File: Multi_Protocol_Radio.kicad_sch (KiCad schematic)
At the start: 6 parts, among them J2001 TC2050, J2002 Conn_01x06_Pin, J2003 Conn_01x06_Pin, U2001 MGM240PB32VNA3

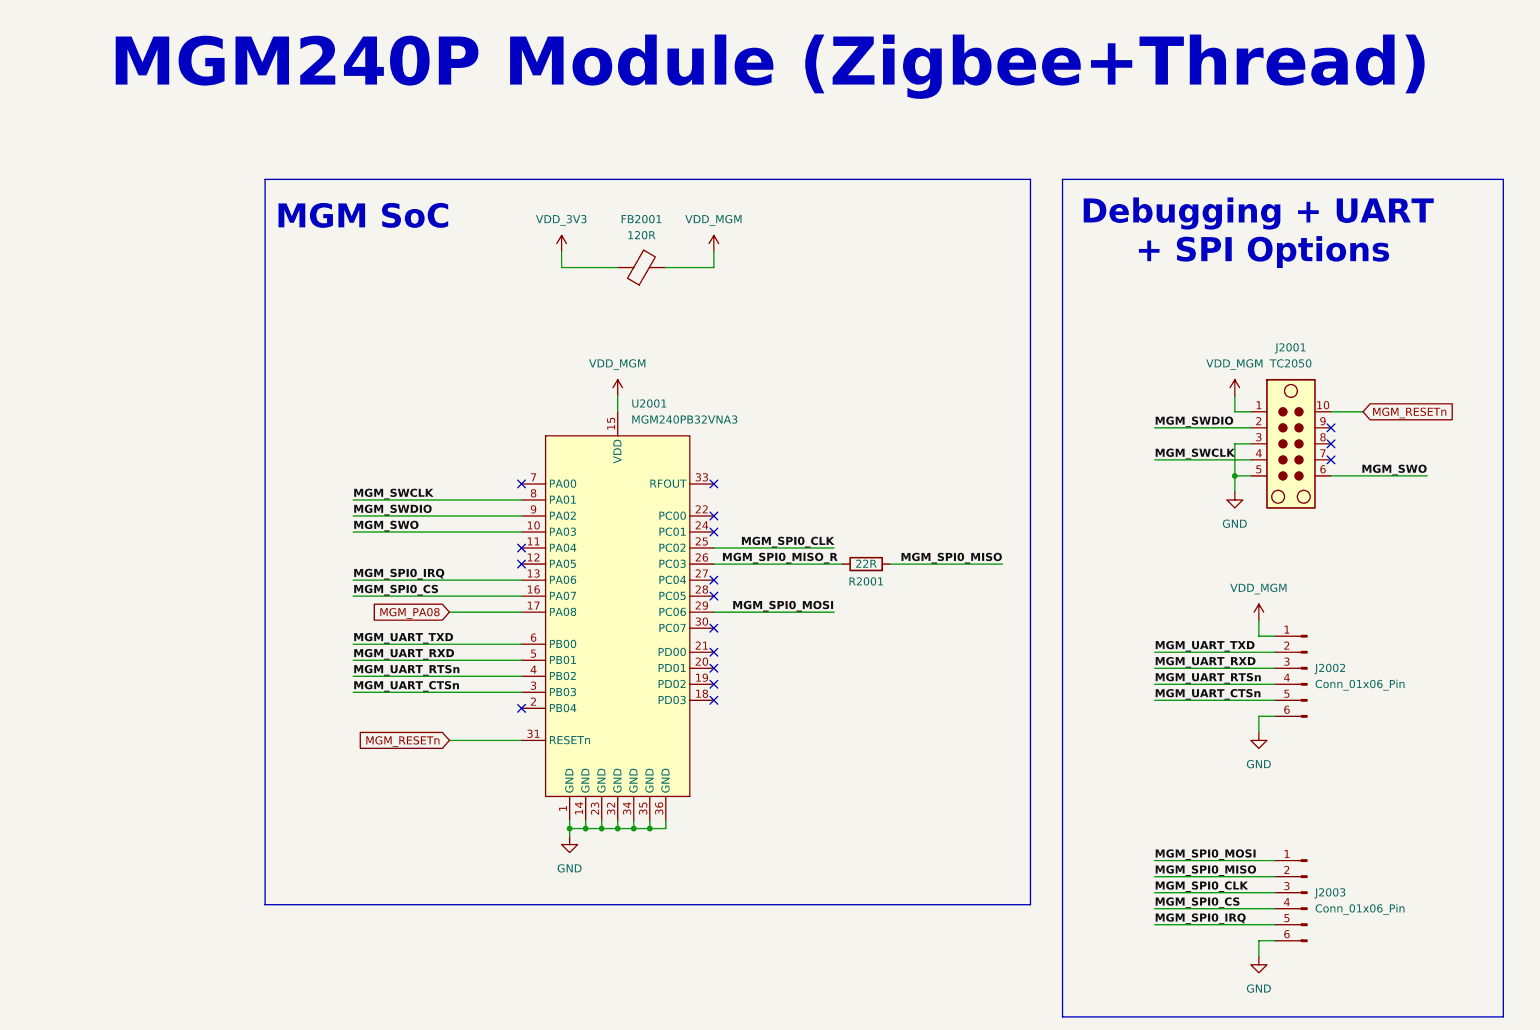
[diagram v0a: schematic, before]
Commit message: All JLC part numbers added to BOM except LEDs
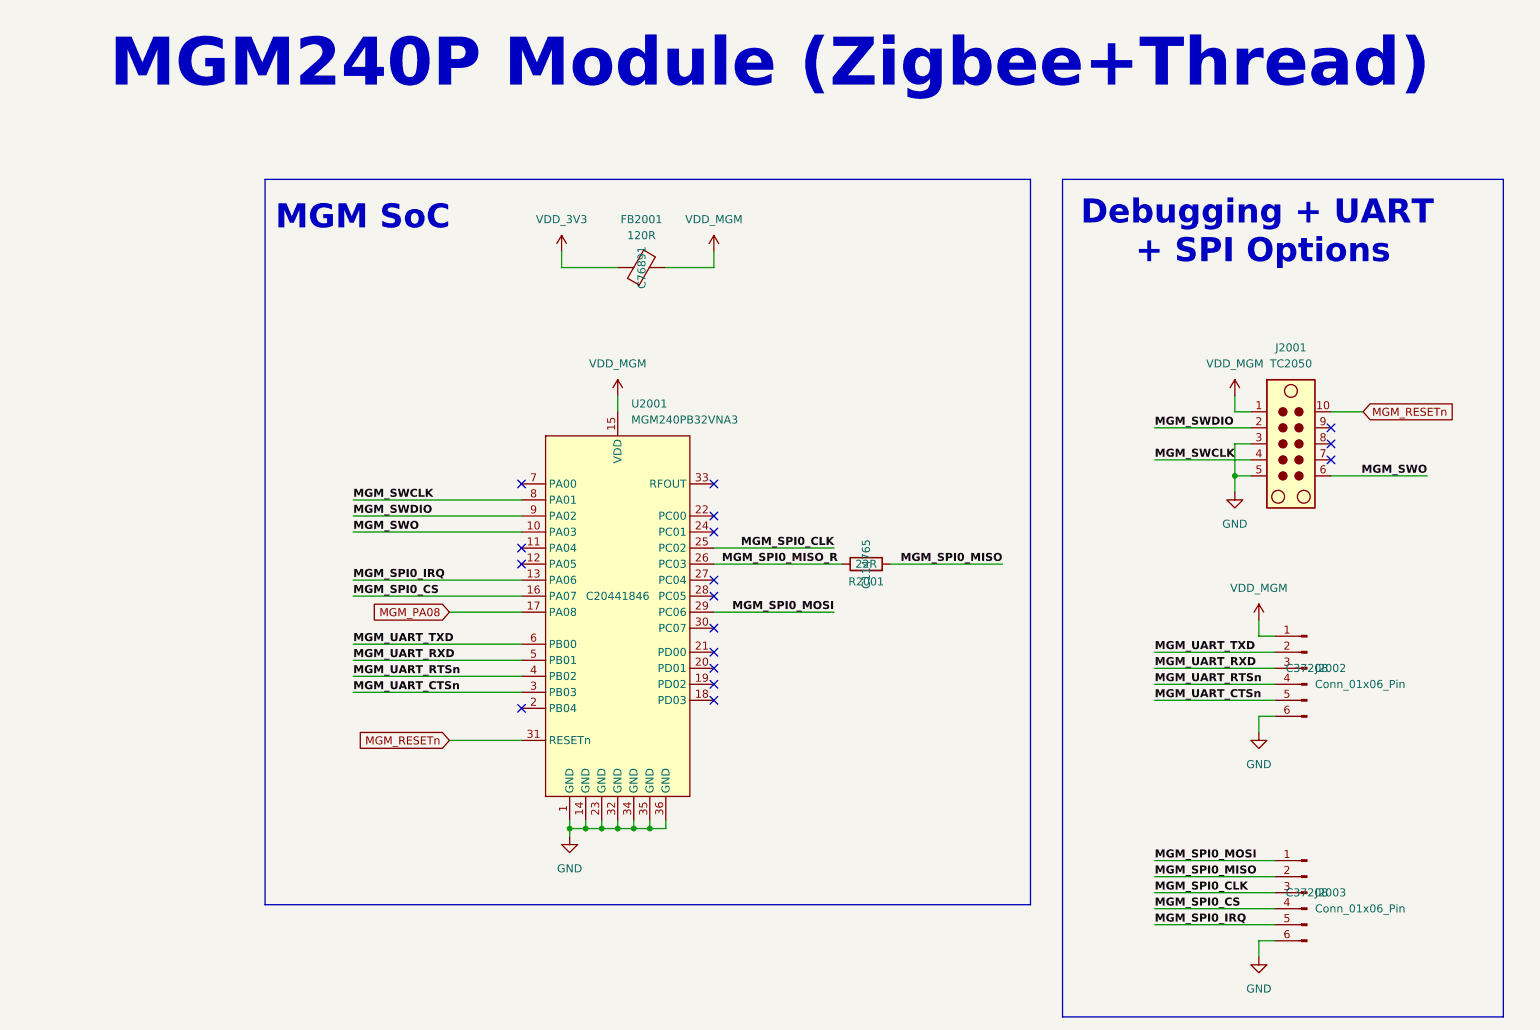
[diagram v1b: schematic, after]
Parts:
- FB2001: JLCPCB Part# (none) -> C76891
- J2002, J2003: JLCPCB Part# (none) -> C37208
- R2001: JLCPCB Part# (none) -> C114765
- U2001: JLCPCB Part# (none) -> C20441846
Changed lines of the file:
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@@
 			)
 		)
-		(property "JLCPCB Part#" ""
+		(property "JLCPCB Part#" "C37208"
 			(at 214.63 158.75 0)
 			(effects
@@
 			)
 		)
-		(property "JLCPCB Part#" ""
+		(property "JLCPCB Part#" "C20441846"
 			(at 105.41 111.76 0)
 			(effects
@@
 			)
 		)
-		(property "JLCPCB Part#" ""
+		(property "JLCPCB Part#" "C76891"
 			(at 109.22 59.69 0)
 			(effects
@@
 			)
 		)
-		(property "JLCPCB Part#" ""
+		(property "JLCPCB Part#" "C37208"
 			(at 214.63 123.19 0)
 			(effects
@@
 			)
 		)
-		(property "JLCPCB Part#" ""
+		(property "JLCPCB Part#" "C114765"
 			(at 144.78 106.68 0)
 			(effects

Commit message: Small DDR4 cleanup
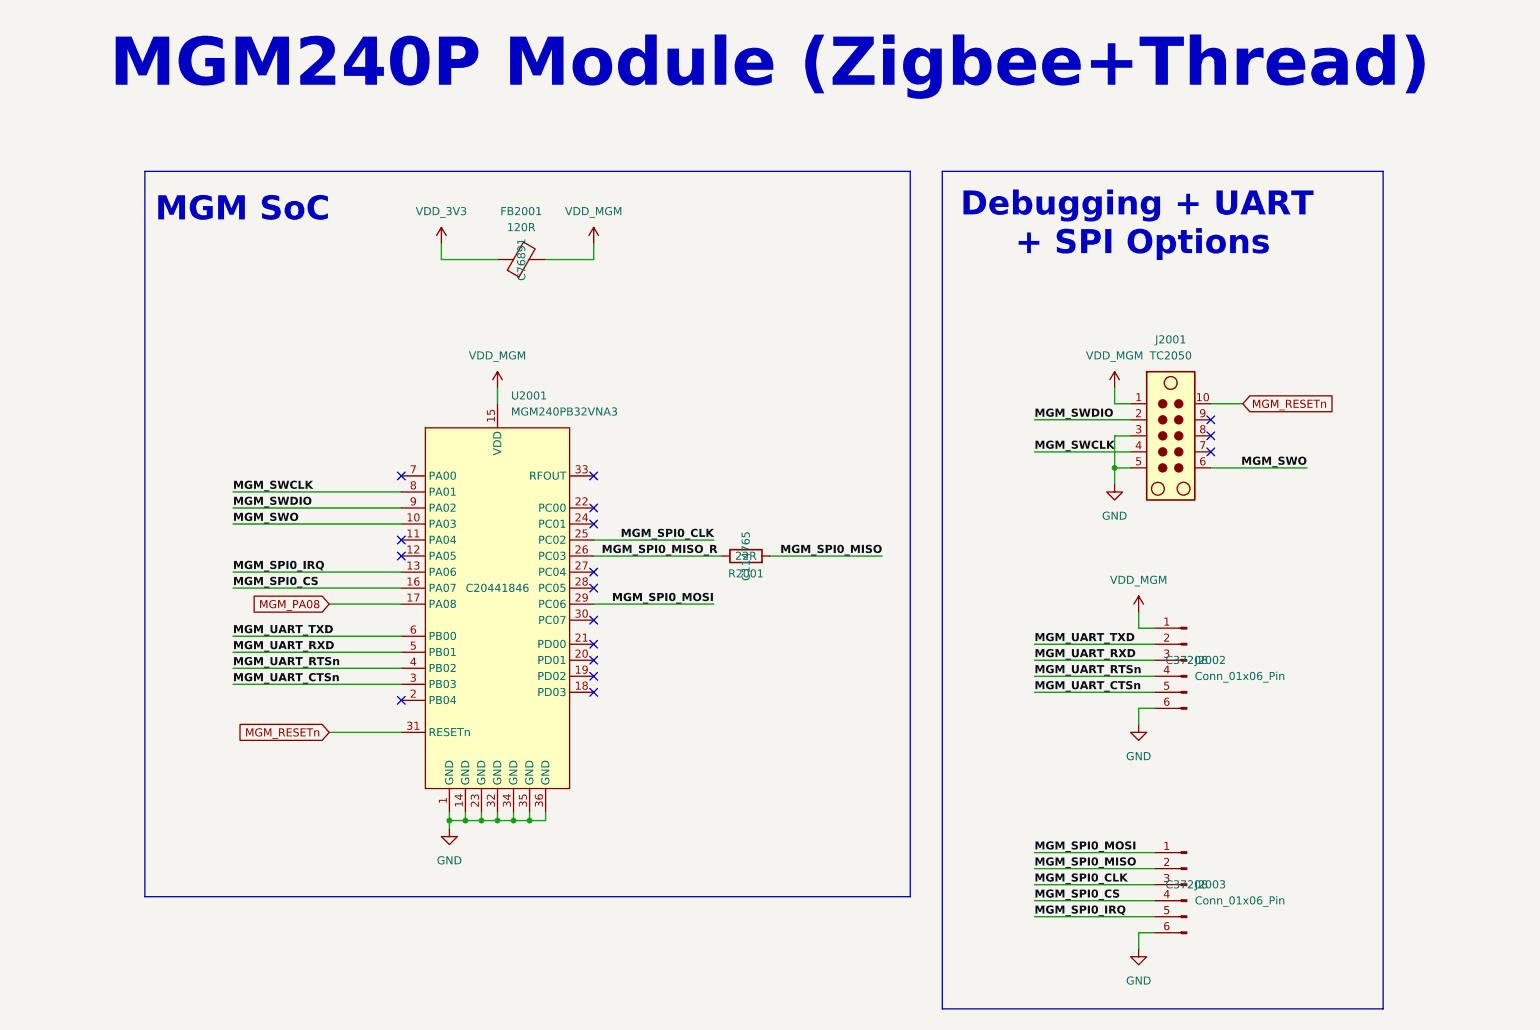
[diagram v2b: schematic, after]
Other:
- moved on the sheet: FB2001, J2001, J2002, J2003, R2001, U2001

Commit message: Added extra decoupling capacitors and pull up resistor to MGM240P module
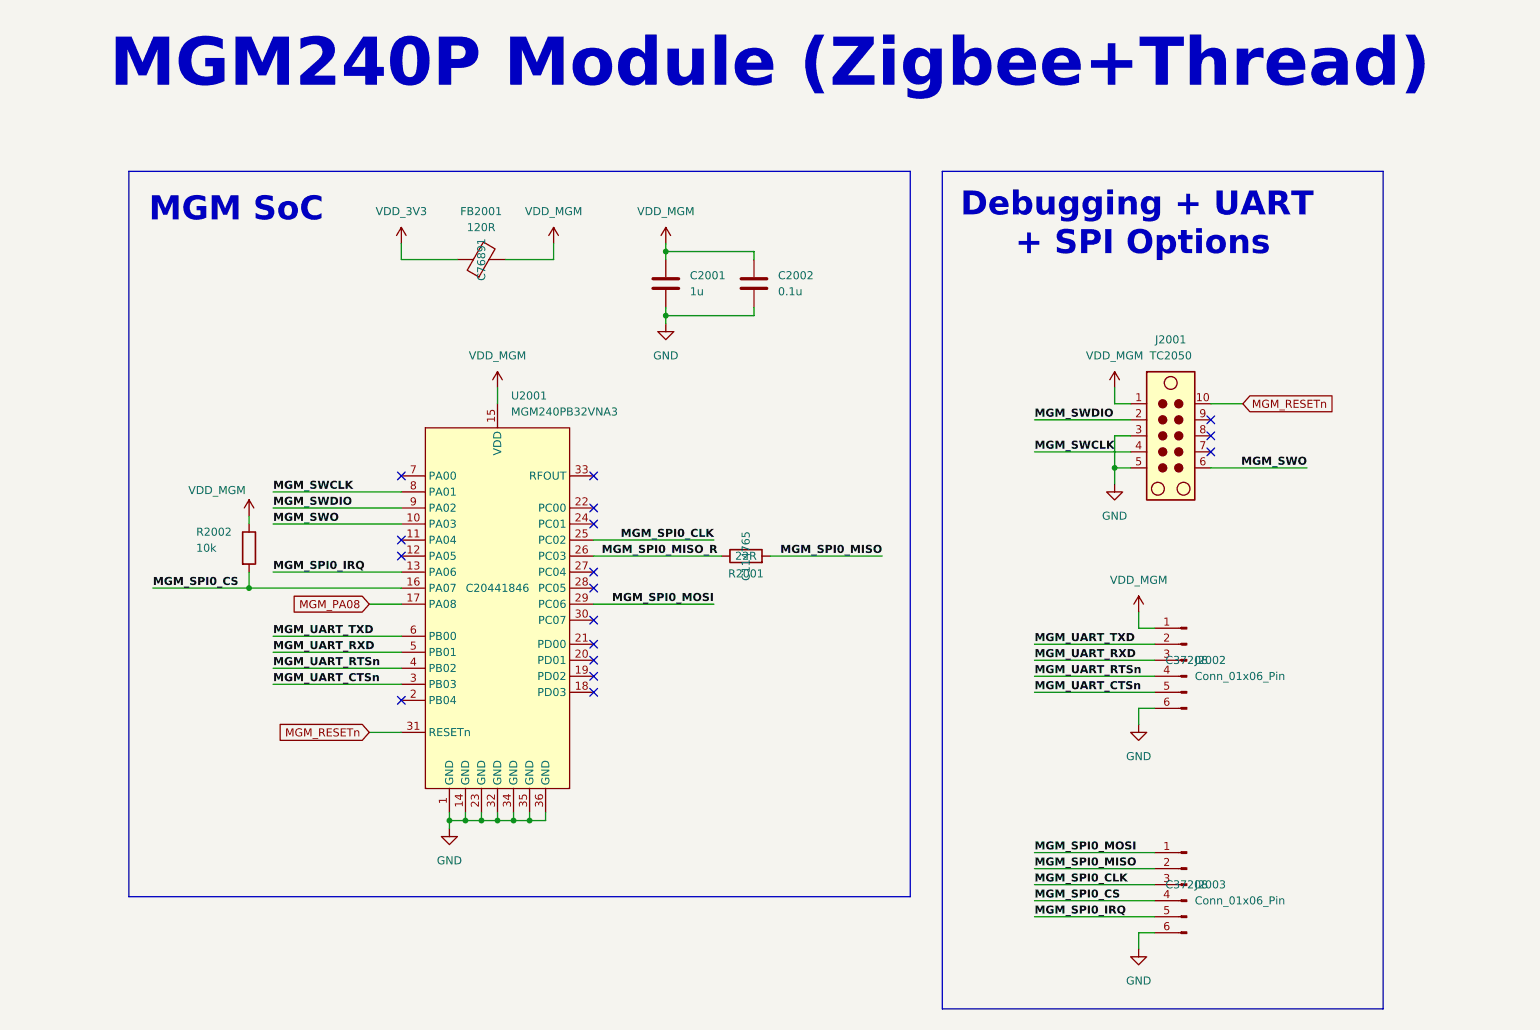
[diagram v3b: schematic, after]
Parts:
- added C2001: 1u, Capacitor_SMD:C_0402_1005Metric, symbol Device:C
- added C2002: 0.1u, Capacitor_SMD:C_0402_1005Metric, symbol Device:C
- added R2002: 10k, Resistor_SMD:R_0402_1005Metric, symbol Device:R
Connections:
- net GND: now also C2001.2, C2002.2
- net MGM_SPI0_CS: now also R2002.2
- net VDD_MGM: now also C2001.1, C2002.1, R2002.1
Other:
- moved on the sheet: FB2001

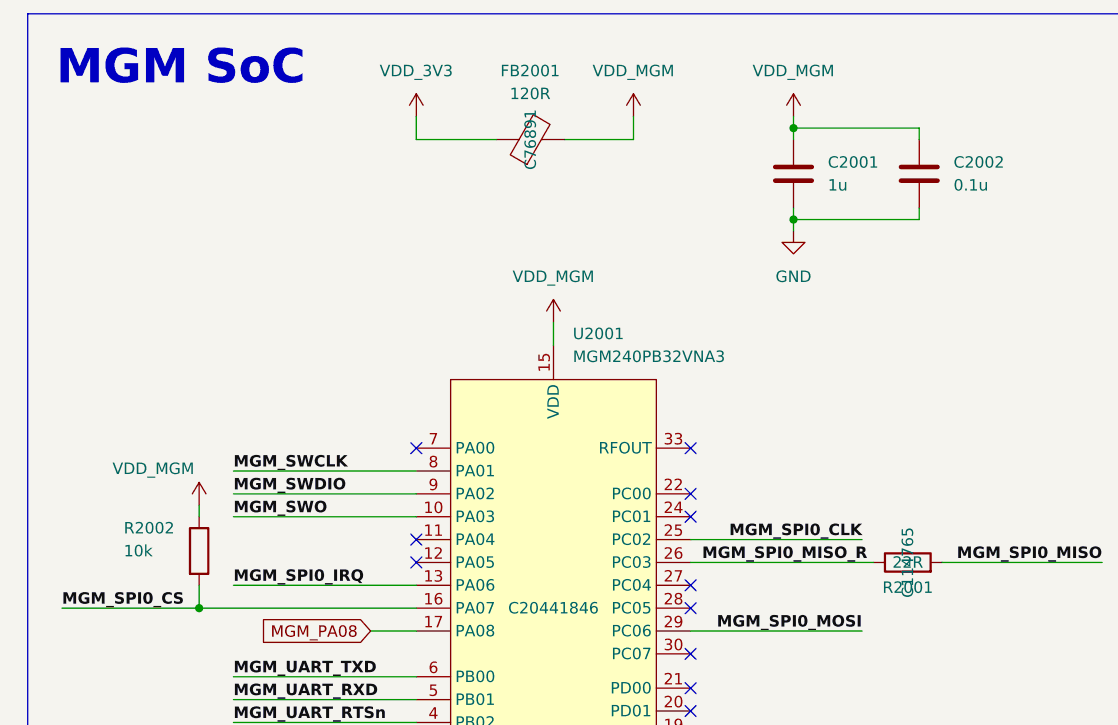
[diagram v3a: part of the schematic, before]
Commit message: Updated JLC part numbers
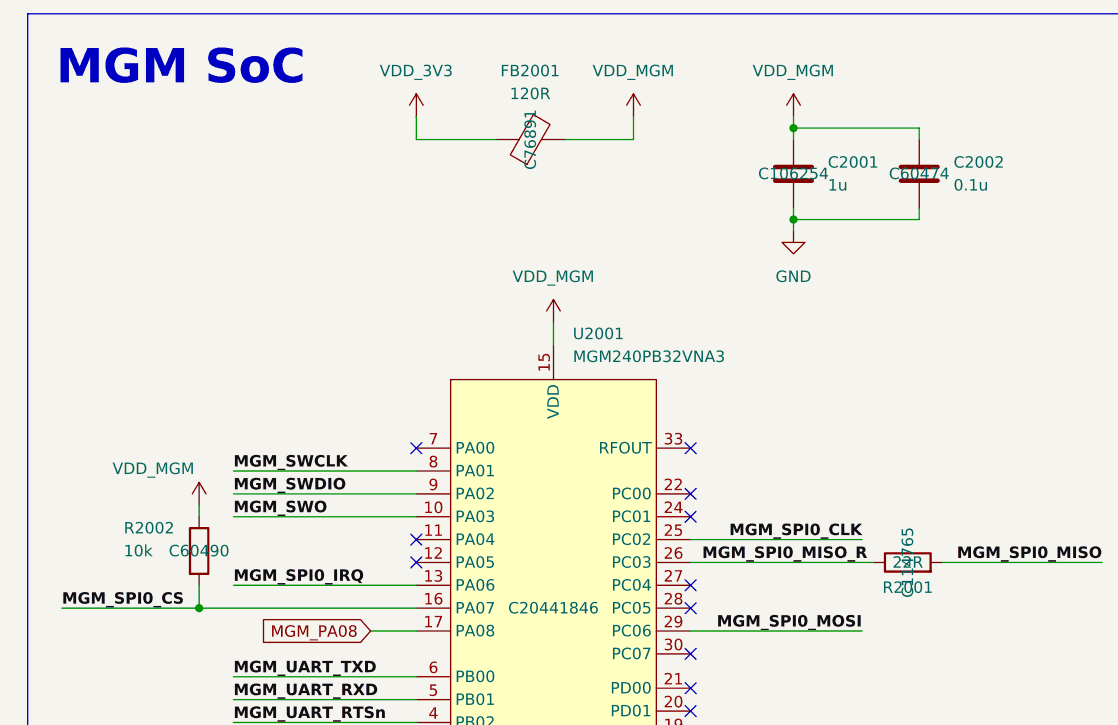
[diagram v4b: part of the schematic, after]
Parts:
- C2001: JLCPCB Part# (none) -> C106254
- C2002: JLCPCB Part# (none) -> C60474
- R2002: JLCPCB Part# (none) -> C60490
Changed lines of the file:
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@@
+			)
+		)
+		(property "JLCPCB Part#" "C60490"
+			(at 46.99 104.14 0)
+			(effects
+				(font
+					(size 1.27 1.27)
+				)
 			)
 		)
@@
 				)
 				(hide yes)
+			)
+		)
+		(property "JLCPCB Part#" "C60474"
+			(at 127 62.23 0)
+			(effects
+				(font
+					(size 1.27 1.27)
+				)
 			)
 		)
@@
 			)
 		)
+		(property "JLCPCB Part#" " C106254"
+			(at 113.03 62.23 0)
+			(effects
+				(font
+					(size 1.27 1.27)
+				)
+			)
+		)

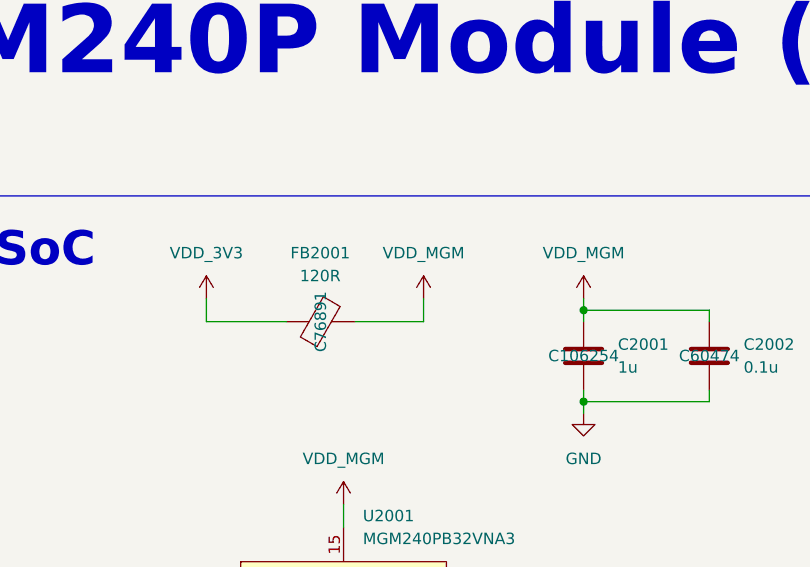
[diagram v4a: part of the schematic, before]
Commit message: Fixed RESETSTATz shorted to ground
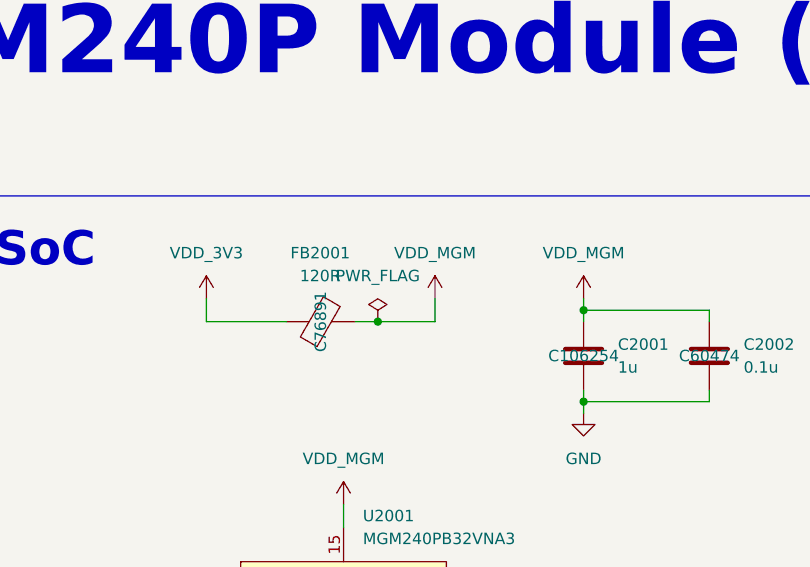
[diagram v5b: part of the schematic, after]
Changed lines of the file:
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@@
+	)
+	(junction
+		(at 90.17 58.42)
+		(diameter 0)
+		(color 0 0 0 0)
 	)
 	(junction
@@
 	(wire
 		(pts
+			(xy 90.17 58.42) (xy 96.52 58.42)
+		)
+		(stroke
+			(width 0)
+			(type default)
+		)
+	)
+	(wire
+		(pts
 			(xy 113.03 67.31) (xy 113.03 68.58)
 		)
@@
 	(wire
 		(pts
-			(xy 95.25 58.42) (xy 95.25 55.88)
+			(xy 96.52 58.42) (xy 96.52 55.88)
 		)
 		(stroke
@@
 	(wire
 		(pts
-			(xy 87.63 58.42) (xy 95.25 58.42)
+			(xy 87.63 58.42) (xy 90.17 58.42)
 		)
 		(stroke
@@
 	(symbol
 		(lib_id "power:VDD")
-		(at 95.25 55.88 0)
+		(at 96.52 55.88 0)
 		(unit 1)
 		(exclude_from_sim no)
@@
 		(fields_autoplaced yes)
 		(property "Reference" "#PWR02002"
-			(at 95.25 59.69 0)
+			(at 96.52 59.69 0)
 			(effects
 				(font
@@
 		)
 		(property "Value" "VDD_MGM"
-			(at 95.25 50.8 0)
+			(at 96.52 50.8 0)
 			(effects
 				(font
@@
 		)
 		(property "Footprint" ""
-			(at 95.25 55.88 0)
+			(at 96.52 55.88 0)
 			(effects
 				(font
@@
 		)
 		(property "Datasheet" ""
-			(at 95.25 55.88 0)
+			(at 96.52 55.88 0)
 			(effects
 				(font
@@
 		)
 		(property "Description" "Power symbol creates a global label with name \"VDD\""
-			(at 95.25 55.88 0)
+			(at 96.52 55.88 0)
 			(effects
 				(font
@@
 					(unit 1)
 				)
+			)
+		)
+	)
+	(symbol
+		(lib_id "power:PWR_FLAG")
+		(at 90.17 58.42 0)
+		(unit 1)
+		(exclude_from_sim no)
+		(in_bom yes)
+		(on_board yes)
+		(dnp no)
+		(fields_autoplaced yes)
+		(property "Reference" "#FLG02001"
+			(at 90.17 56.515 0)
+			(effects
+				(font
+					(size 1.27 1.27)
+				)
+				(hide yes)
+			)
+		)
+		(property "Value" "PWR_FLAG"
+			(at 90.17 53.34 0)
+			(effects
+				(font
+					(size 1.27 1.27)
+				)
+			)
+		)
+		(property "Footprint" ""
+			(at 90.17 58.42 0)
+			(effects
+				(font
+					(size 1.27 1.27)
+				)
+				(hide yes)
+			)
+		)
+		(property "Datasheet" "~"
+			(at 90.17 58.42 0)
+			(effects
+				(font
+					(size 1.27 1.27)
+				)
+				(hide yes)
+			)
+		)
+		(property "Description" "Special symbol for telling ERC where power comes from"
+			(at 90.17 58.42 0)
+			(effects
+				(font
+					(size 1.27 1.27)
+				)
+				(hide yes)
+			)
+		)
+		(pin "1"
+		)
+		(instances
+			(project ""
+				(path "/b43b7bca-e50d-42ec-8ff0-e0016dfefe0a/a72e3651-6b85-4045-b319-d8959d969ced"
+					(reference "#FLG02001")
+					(unit 1)
+				)
